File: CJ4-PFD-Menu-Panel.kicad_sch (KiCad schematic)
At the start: 31 parts, among them J1 Conn_01x02, J8 Conn_01x02, SW10 SW_PUSH_LED, SW11 SW_PUSH_LED, SW12 SW_PUSH_LED, SW13 SW_PUSH_LED, SW3 SW_PUSH_LED, SW4 SW_PUSH_LED, SW5 SW_PUSH_LED, SW6 SW_PUSH_LED, SW7 SW_PUSH_LED, SW8 SW_PUSH_LED, SW9 SW_PUSH_LED, U1 DM13A

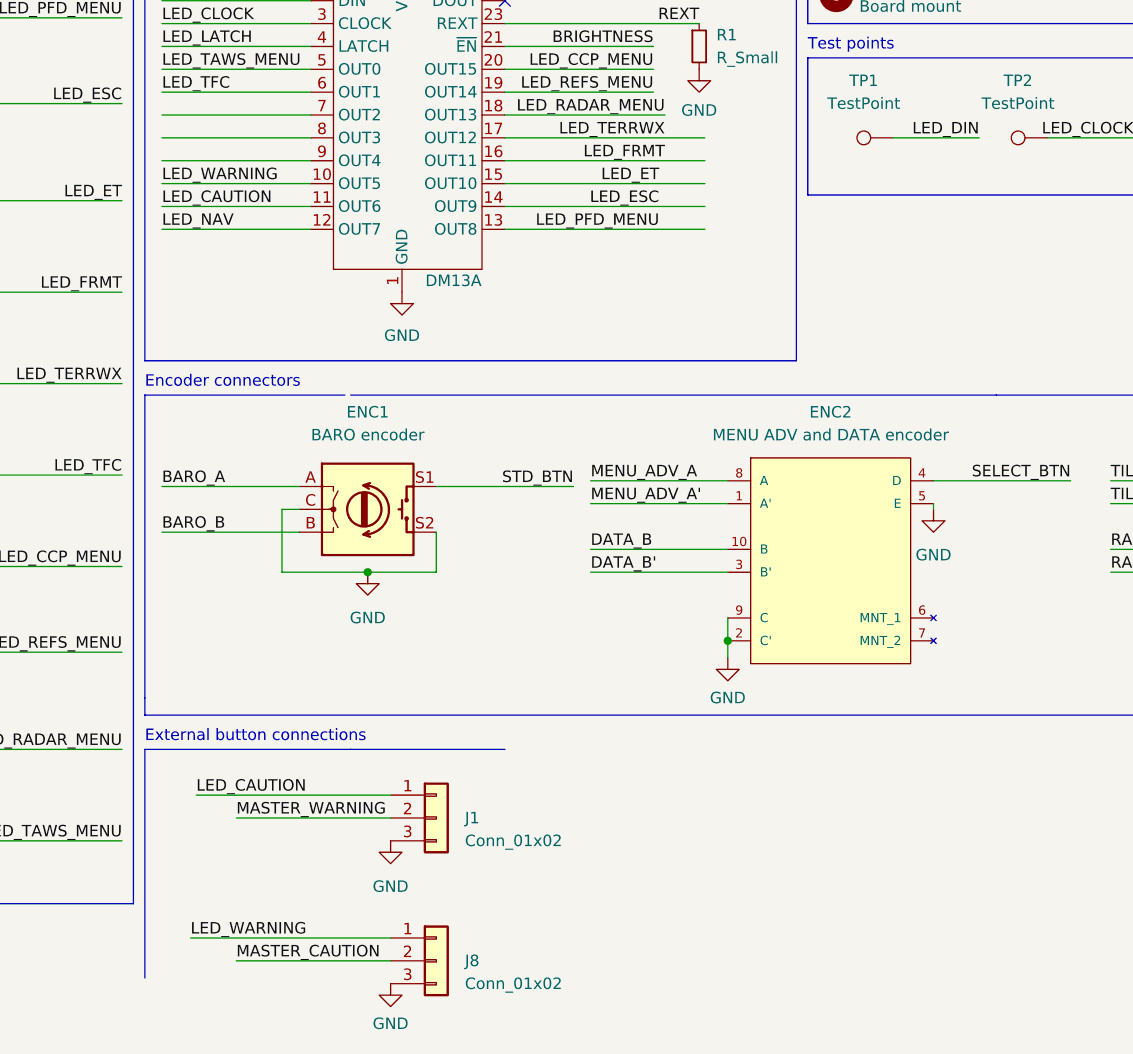
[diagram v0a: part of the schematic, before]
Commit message: Update external button connector, 3d models
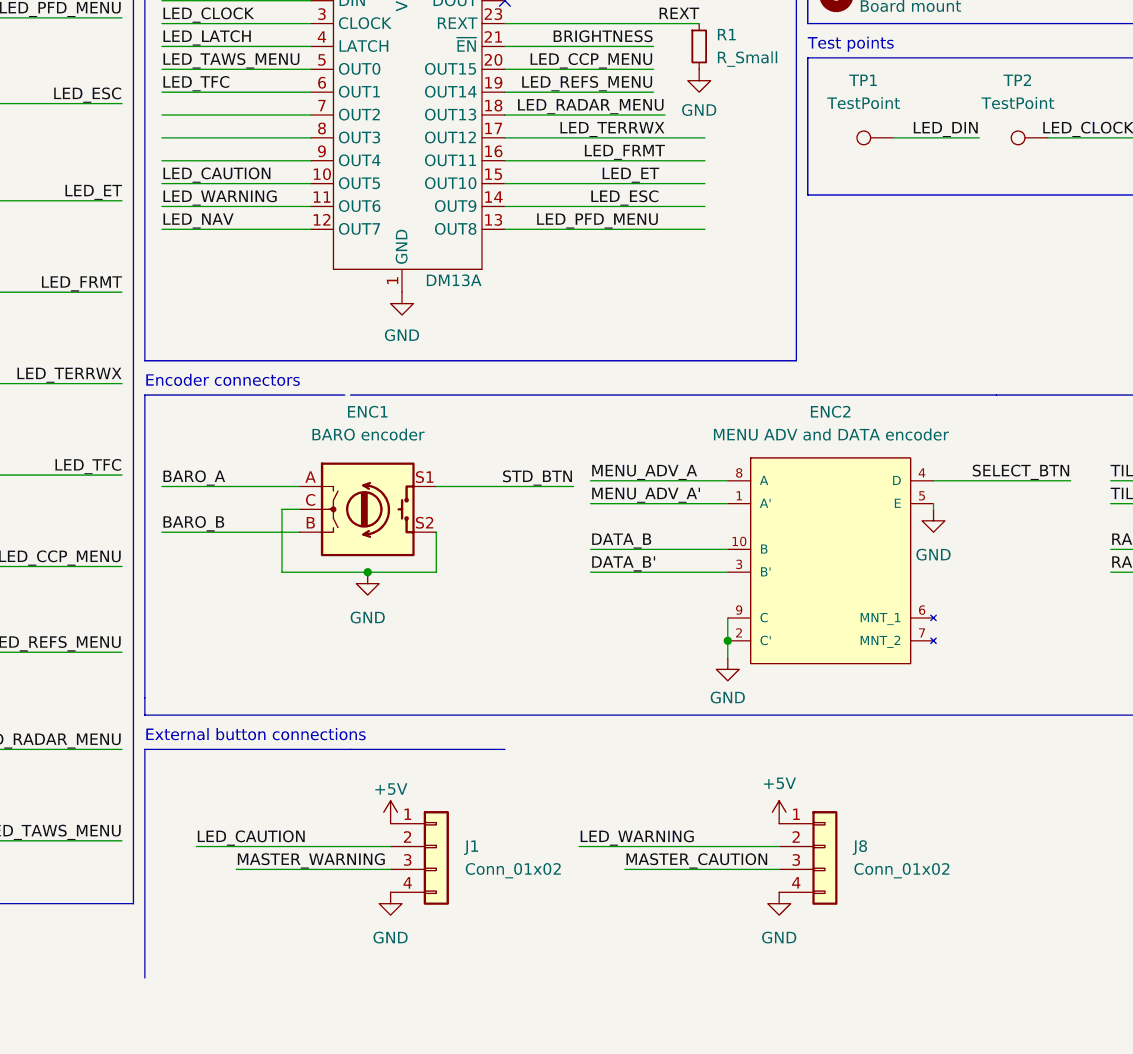
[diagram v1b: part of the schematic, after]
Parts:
- J1, J8: footprint Connector_JST:JST_XH_B3B-XH-A_1x03_P2.50mm_Vertical -> Connector_JST:JST_XH_B4B-XH-A_1x04_P2.50mm_Vertical; symbol Connector_Generic:Conn_01x03 -> Connector_Generic:Conn_01x04
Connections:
- net GND: now also J1.4 (Pin_4), J8.4 (Pin_4); no longer J1.3 (Pin_3), J8.3 (Pin_3)
- net LED_CAUTION: now also J1.2 (Pin_2), U1.10 (OUT5); no longer J1.1 (Pin_1), U1.11 (OUT6)
- net LED_WARNING: now also J8.2 (Pin_2), U1.11 (OUT6); no longer J8.1 (Pin_1), U1.10 (OUT5)
- net MASTER_CAUTION: now also J8.3 (Pin_3); no longer J8.2 (Pin_2)
- net MASTER_WARNING: now also J1.3 (Pin_3); no longer J1.2 (Pin_2)
- new net +5V: J1.1 (Pin_1), J8.1 (Pin_1)

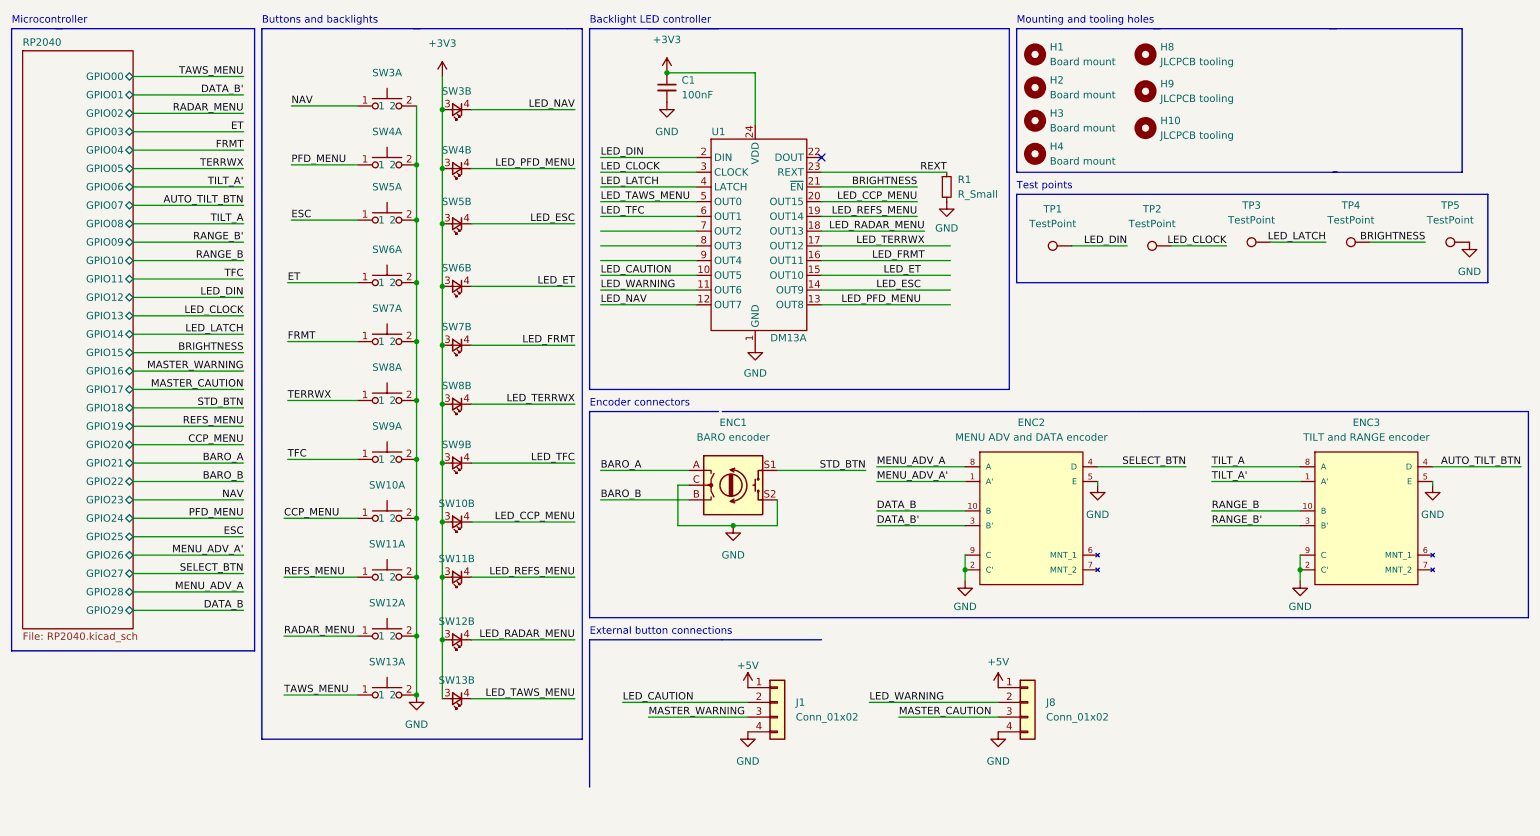
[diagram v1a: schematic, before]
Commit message: Cleanup silkscreen and version/date
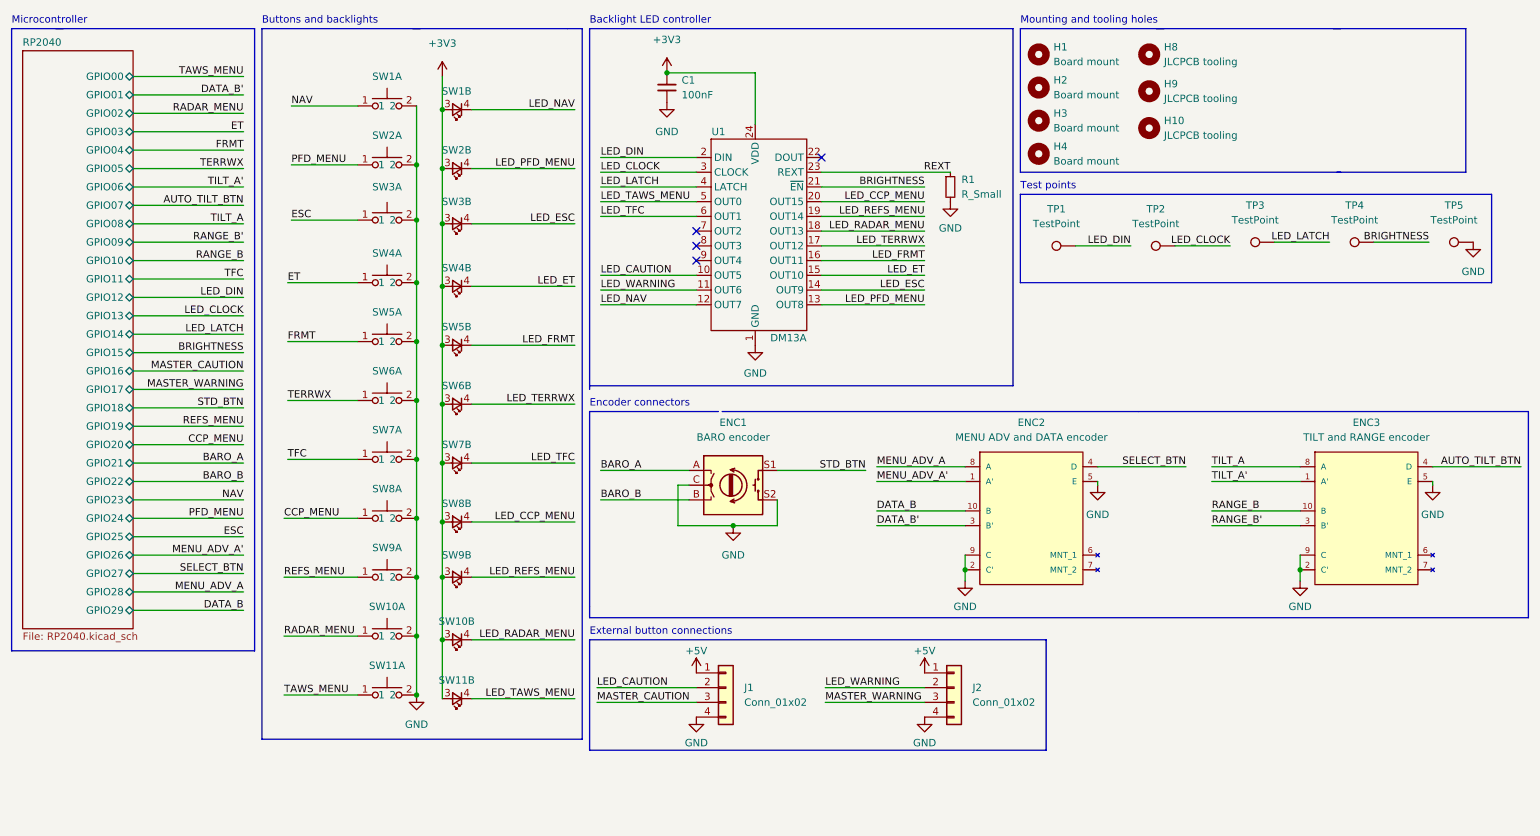
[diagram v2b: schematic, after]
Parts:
- renumbered J8 to J2, SW3 to SW1, SW12 to SW10, SW13 to SW11, SW4 to SW2, SW5 to SW3, SW6 to SW4, SW7 to SW5, SW8 to SW6, SW9 to SW7, SW10 to SW8, SW11 to SW9
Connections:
- net MASTER_CAUTION: now also J1.3 (Pin_3); no longer J2.3 (Pin_3)
- net MASTER_WARNING: now also J2.3 (Pin_3); no longer J1.3 (Pin_3)
- no-connect marks 1 -> 4
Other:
- moved on the sheet: H1, H10, H2, H3, H4, H8, H9, J1, J2, R1, TP1, TP2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

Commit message: Silkscreen and date/version stuff
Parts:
- C1: value 100nF -> 1uF; JLC (none) -> 0402; LCSC (none) -> C52923
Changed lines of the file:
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@@
   (paper "A4")
   (title_block
-    (date "${date}")
-    (rev "${version}")
+    (date "${DATE}")
+    (rev "${VERSION}")
   )
   (junction (at 85.725 39.37) (diameter 0) (color 0 0 0 0)
@@
   (symbol (lib_id "Device:C_Small") (at 128.905 26.035 0) (unit 1)
     (in_bom yes) (on_board yes) (fields_autoplaced)
-    (property "Reference" "C1" (id 0) (at 131.445 24.7712 0)
-      (effects (font (size 1.27 1.27)) (justify left))
-    )
-    (property "Value" "100nF" (id 1) (at 131.445 27.3112 0)
+    (property "Reference" "C1" (id 0) (at 132.08 24.7712 0)
+      (effects (font (size 1.27 1.27)) (justify left))
+    )
+    (property "Value" "1uF" (id 1) (at 132.08 27.3112 0)
       (effects (font (size 1.27 1.27)) (justify left))
     )
@@
     )
     (property "Datasheet" "~" (id 3) (at 128.905 26.035 0)
+      (effects (font (size 1.27 1.27)) hide)
+    )
+    (property "JLC" "0402" (id 4) (at 128.905 26.035 0)
+      (effects (font (size 1.27 1.27)) hide)
+    )
+    (property "LCSC" "C52923" (id 5) (at 128.905 26.035 0)
       (effects (font (size 1.27 1.27)) hide)
     )
@@
     )
     (path "/935a56df-84d4-49db-855e-593d55487c2c"
-      (reference "C1") (unit 1) (value "100nF") (footprint "Custom_Footprints:Perfect_0402")
+      (reference "C1") (unit 1) (value "1uF") (footprint "Custom_Footprints:Perfect_0402")
     )
     (path "/f2c43eeb-76da-49f4-b8e6-cd74ebb3190b/52cf6701-e0f8-4481-827c-0fbd4e9bec67"
@@
     )
     (path "/f2c43eeb-76da-49f4-b8e6-cd74ebb3190b/d231b70d-8a29-4e78-a17c-75abb025b07e"
-      (reference "C7") (unit 1) (value "1uF") (footprint "Capacitor_SMD:C_0603_1608Metric")
+      (reference "C7") (unit 1) (value "1uF") (footprint "Custom_Footprints:Perfect_0402")
     )
     (path "/f2c43eeb-76da-49f4-b8e6-cd74ebb3190b/4d7a5022-36cd-4f67-bb82-a9afd32a776e"
-      (reference "C8") (unit 1) (value "100nF") (footprint "Custom_Footprints:Perfect_0402")
+      (reference "C8") (unit 1) (value "1uF") (footprint "Custom_Footprints:Perfect_0402")
     )
     (path "/f2c43eeb-76da-49f4-b8e6-cd74ebb3190b/45801e50-45ec-4892-af18-34a3e6ab3fad"
-      (reference "C9") (unit 1) (value "1uF") (footprint "Capacitor_SMD:C_0603_1608Metric")
+      (reference "C9") (unit 1) (value "1uF") (footprint "Custom_Footprints:Perfect_0402")
     )
     (path "/f2c43eeb-76da-49f4-b8e6-cd74ebb3190b/f7e200ad-0805-42f5-9f32-792f4044fcf7"

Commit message: Fix encoder wiring
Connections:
- net DATA_B renamed MENU_ADV_B
- net MENU_ADV_A' renamed DATA_A'
- net RANGE_B renamed TILT_B
- net TILT_A' renamed RANGE_A'
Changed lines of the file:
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@@
     (effects (font (size 1.27 1.27)) (justify right bottom))
   )
-  (label "RANGE_B" (at 55.88 55.88 180)
+  (label "TILT_B" (at 55.88 55.88 180)
     (effects (font (size 1.27 1.27)) (justify right bottom))
   )
@@
     (effects (font (size 1.27 1.27)) (justify left bottom))
   )
-  (label "RANGE_B" (at 222.885 99.06 0)
-    (effects (font (size 1.27 1.27)) (justify left bottom))
-  )
-  (label "DATA_B" (at 55.88 116.205 180)
+  (label "TILT_B" (at 222.885 99.06 0)
+    (effects (font (size 1.27 1.27)) (justify left bottom))
+  )
+  (label "MENU_ADV_B" (at 55.88 116.205 180)
     (effects (font (size 1.27 1.27)) (justify right bottom))
   )
@@
     (effects (font (size 1.27 1.27)) (justify left bottom))
   )
-  (label "DATA_B" (at 165.1 99.06 0)
+  (label "MENU_ADV_B" (at 165.1 99.06 0)
     (effects (font (size 1.27 1.27)) (justify left bottom))
   )
@@
     (effects (font (size 1.27 1.27)) (justify right bottom))
   )
-  (label "TILT_A'" (at 222.885 93.98 0)
+  (label "RANGE_A'" (at 222.885 93.98 0)
     (effects (font (size 1.27 1.27)) (justify left bottom))
   )
@@
     (effects (font (size 1.27 1.27)) (justify left bottom))
   )
-  (label "TILT_A'" (at 55.88 43.18 180)
+  (label "RANGE_A'" (at 55.88 43.18 180)
     (effects (font (size 1.27 1.27)) (justify right bottom))
   )
@@
     (effects (font (size 1.27 1.27)) (justify right bottom))
   )
-  (label "MENU_ADV_A'" (at 165.1 93.98 0)
+  (label "DATA_A'" (at 165.1 93.98 0)
     (effects (font (size 1.27 1.27)) (justify left bottom))
   )
@@
     (effects (font (size 1.27 1.27)) (justify right bottom))
   )
-  (label "MENU_ADV_A'" (at 55.88 106.68 180)
-    (effects (font (size 1.27 1.27)) (justify right bottom))
-  )
+  (label "DATA_A'" (at 55.88 106.68 180)
+    (effects (font (size 1.27 1.27)) (justify right bottom))
+  )

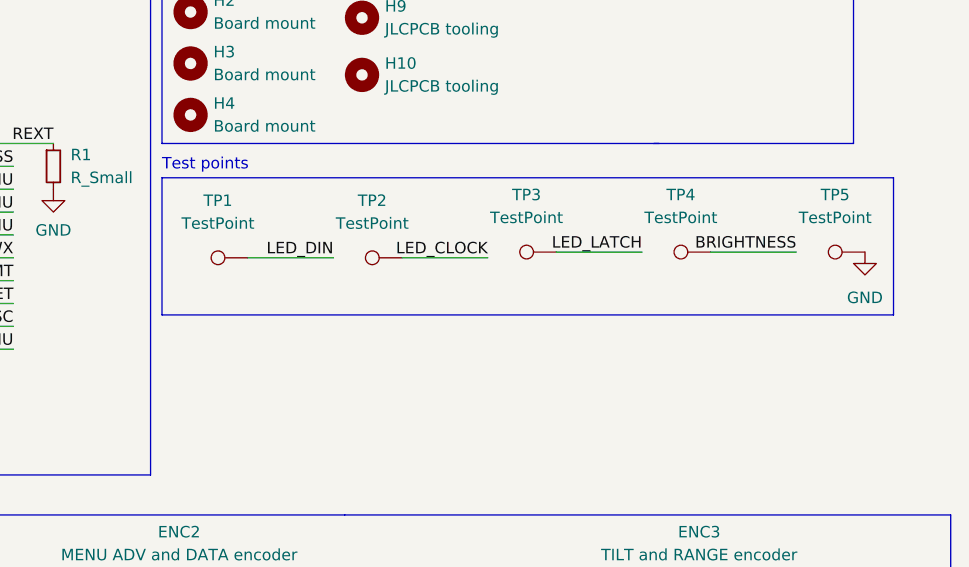
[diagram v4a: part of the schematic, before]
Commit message: Add debug connections
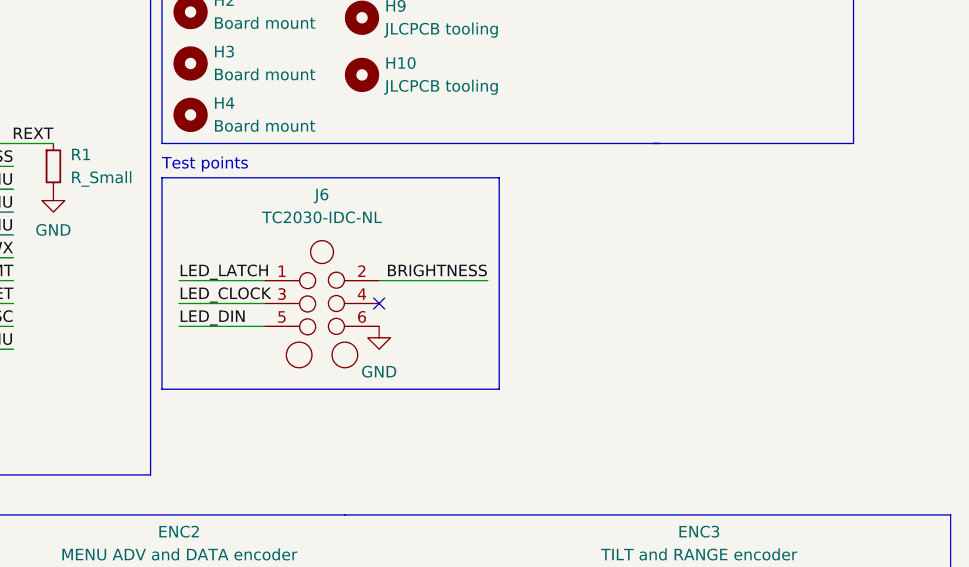
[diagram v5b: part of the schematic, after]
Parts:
- removed TP1, TP2, TP3, TP4, TP5: TestPoint, TestPoint:TestPoint_Keystone_5000-5004_Miniature, symbol Connector:TestPoint
- added J6: TC2030-IDC-NL, Connector:Tag-Connect_TC2030-IDC-NL_2x03_P1.27mm_Vertical, symbol Tag-Connect:TC2030-IDC-NL
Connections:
- net BRIGHTNESS: now also J6.2 (Pin_2)
- net GND: now also J6.6 (Pin_6)
- net LED_CLOCK: now also J6.3 (Pin_3)
- net LED_DIN: now also J6.5 (Pin_5)
- net LED_LATCH: now also J6.1 (Pin_1)
- no-connect marks 4 -> 5

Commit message: Final changes prior to ordering
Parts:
- R1: value R_Small -> 3k; footprint Custom_Footprints:Perfect_0402 -> Resistor_SMD:R_0805_2012Metric_Pad1.20x1.40mm_HandSolder; JLC (none) -> 0805; LCSC (none) -> C17661
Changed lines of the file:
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@@
   (symbol (lib_id "Device:R_Small") (at 177.8 43.18 0) (unit 1)
     (in_bom yes) (on_board yes) (fields_autoplaced)
-    (property "Reference" "R1" (id 0) (at 179.705 41.9099 0)
-      (effects (font (size 1.27 1.27)) (justify left))
-    )
-    (property "Value" "R_Small" (id 1) (at 179.705 44.4499 0)
-      (effects (font (size 1.27 1.27)) (justify left))
-    )
-    (property "Footprint" "Custom_Footprints:Perfect_0402" (id 2) (at 177.8 43.18 0)
+    (property "Reference" "R1" (id 0) (at 180.34 41.9099 0)
+      (effects (font (size 1.27 1.27)) (justify left))
+    )
+    (property "Value" "3k" (id 1) (at 180.34 44.4499 0)
+      (effects (font (size 1.27 1.27)) (justify left))
+    )
+    (property "Footprint" "Resistor_SMD:R_0805_2012Metric_Pad1.20x1.40mm_HandSolder" (id 2) (at 177.8 43.18 0)
       (effects (font (size 1.27 1.27)) hide)
     )
     (property "Datasheet" "~" (id 3) (at 177.8 43.18 0)
+      (effects (font (size 1.27 1.27)) hide)
+    )
+    (property "JLC" "0805" (id 4) (at 177.8 43.18 0)
+      (effects (font (size 1.27 1.27)) hide)
+    )
+    (property "LCSC" "C17661" (id 5) (at 177.8 43.18 0)
       (effects (font (size 1.27 1.27)) hide)
     )
@@
       (reference "#PWR042") (unit 1) (value "GND") (footprint "")
     )
-    (path "/f2c43eeb-76da-49f4-b8e6-cd74ebb3190b/7a57c193-8053-4916-9ab0-4158f2cee9c7"
-      (reference "#PWR0101") (unit 1) (value "GND") (footprint "")
-    )
     (path "/f2c43eeb-76da-49f4-b8e6-cd74ebb3190b/9a22861a-f0d5-45ff-9510-d64aac14d2d5"
       (reference "#PWR0102") (unit 1) (value "GND") (footprint "")
@@
     )
     (path "/178a1d26-b45f-4eb6-866a-0570a0a1d0b5"
-      (reference "R1") (unit 1) (value "R_Small") (footprint "Custom_Footprints:Perfect_0402")
+      (reference "R1") (unit 1) (value "3k") (footprint "Resistor_SMD:R_0805_2012Metric_Pad1.20x1.40mm_HandSolder")
     )
     (path "/f2c43eeb-76da-49f4-b8e6-cd74ebb3190b/8f83e7e3-f3a2-4d64-8dcf-30acf74c6e09"
@@
       (reference "U1") (unit 1) (value "DM13A") (footprint "Package_SO:SSOP-24_3.9x8.7mm_P0.635mm")
     )
-    (path "/f2c43eeb-76da-49f4-b8e6-cd74ebb3190b/0c8c7e27-e47b-4e84-a415-d07b5eda3657"
-      (reference "U2") (unit 1) (value "XC6206P332MR") (footprint "Package_TO_SOT_SMD:SOT-23")
+    (path "/f2c43eeb-76da-49f4-b8e6-cd74ebb3190b/a7e4ce5c-98fb-48d0-9ff3-cdec8a457bcf"
+      (reference "U2") (unit 1) (value "AMS1117-3.3") (footprint "Package_TO_SOT_SMD:SOT-223-3_TabPin2")
     )
     (path "/f2c43eeb-76da-49f4-b8e6-cd74ebb3190b/c5576968-737d-44d3-a965-13d04b7e79e3"
